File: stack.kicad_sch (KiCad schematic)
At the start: 23 parts, among them U43 74LS193, U46 74LS193, U56 74HCT00, U7 74HCT245

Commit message: changed symbols
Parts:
- U43, U46: symbol 74xx:74LS193 -> 01_my_library:74HCT193
- U7: symbol 74xx:74HC245 -> 01_my_library:74HCT245
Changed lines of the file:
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@@
     )
   )
-  (symbol (lib_id "74xx:74LS193") (at 162.56 104.14 270) (unit 1)
+  (symbol (lib_id "01_my_library:74HCT193") (at 161.29 104.14 270) (unit 1)
     (in_bom yes) (on_board yes) (dnp no) (fields_autoplaced)
     (property "Reference" "U46" (at 180.34 97.2119 90)
@@
       (effects (font (size 1.27 1.27)))
     )
-    (property "Footprint" "" (at 162.56 104.14 0)
-      (effects (font (size 1.27 1.27)) hide)
-    )
-    (property "Datasheet" "http://www.ti.com/lit/ds/symlink/sn74ls193.pdf" (at 162.56 104.14 0)
+    (property "Footprint" "" (at 161.29 104.14 0)
+      (effects (font (size 1.27 1.27)) hide)
+    )
+    (property "Datasheet" "https://www.ti.com/lit/ds/symlink/cd74hct193.pdf?HQS=dis-mous-null-mousermode-dsf-pf-null-wwe&ts=1702791971938&ref_url=https%253A%252F%252Fwww.mouser.be%252F" (at 146.05 104.14 0)
       (effects (font (size 1.27 1.27)) hide)
     )
@@
     )
   )
-  (symbol (lib_id "74xx:74LS193") (at 226.06 104.14 270) (unit 1)
+  (symbol (lib_id "01_my_library:74HCT193") (at 224.79 104.14 270) (unit 1)
     (in_bom yes) (on_board yes) (dnp no) (fields_autoplaced)
     (property "Reference" "U43" (at 243.84 97.2119 90)
@@
       (effects (font (size 1.27 1.27)))
     )
-    (property "Footprint" "" (at 226.06 104.14 0)
-      (effects (font (size 1.27 1.27)) hide)
-    )
-    (property "Datasheet" "http://www.ti.com/lit/ds/symlink/sn74ls193.pdf" (at 226.06 104.14 0)
+    (property "Footprint" "" (at 224.79 104.14 0)
+      (effects (font (size 1.27 1.27)) hide)
+    )
+    (property "Datasheet" "https://www.ti.com/lit/ds/symlink/cd74hct193.pdf?HQS=dis-mous-null-mousermode-dsf-pf-null-wwe&ts=1702791971938&ref_url=https%253A%252F%252Fwww.mouser.be%252F" (at 209.55 104.14 0)
       (effects (font (size 1.27 1.27)) hide)
     )
@@
     )
   )
-  (symbol (lib_id "74xx:74HC245") (at 92.71 104.14 90) (unit 1)
+  (symbol (lib_id "01_my_library:74HCT245") (at 92.71 104.14 90) (unit 1)
     (in_bom yes) (on_board yes) (dnp no)
     (property "Reference" "U7" (at 113.03 97.79 90)
@@
       (effects (font (size 1.27 1.27)) hide)
     )
-    (property "Datasheet" "http://www.ti.com/lit/gpn/sn74HC245" (at 92.71 104.14 0)
-      (effects (font (size 1.27 1.27)) hide)
-    )
+    (property "Datasheet" "https://www.ti.com/lit/ds/symlink/sn74hct245.pdf?ts=1702763405638&ref_url=https%253A%252F%252Fwww.google.com%252F" (at 115.57 104.14 0)
+      (effects (font (size 1.27 1.27)) hide)
+    )

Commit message: some cleanup
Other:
- note added: "I am running out of control signals. I don't see the need to input a stack address, so I am not providing it."
- note removed: "I am running out of control signal. I don't see the need to input a stack address, so I am not providing it."
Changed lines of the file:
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@@
     (stroke (width 0) (type default))
   )
-  (text "I am running out of control signal.\nI don't see the need to input a stack\naddress, so I am not providing it."
+  (text "I am running out of control signals.\nI don't see the need to input a stack\naddress, so I am not providing it."
     (at 245.11 69.85 0)
     (effects (font (size 1.27 1.27)) (justify left bottom))
@@
         )
         (path "/100bb8d1-c3d6-4e1f-87b6-72e4e187243c/77326d47-b417-46cc-a46c-7ab94a8e927d"
-          (reference "#PWR0235") (unit 1)
+          (reference "#PWR0249") (unit 1)
         )
       )
@@
         )
         (path "/100bb8d1-c3d6-4e1f-87b6-72e4e187243c/77326d47-b417-46cc-a46c-7ab94a8e927d"
-          (reference "D118") (unit 1)
+          (reference "D119") (unit 1)
         )
       )
@@
         )
         (path "/100bb8d1-c3d6-4e1f-87b6-72e4e187243c/77326d47-b417-46cc-a46c-7ab94a8e927d"
-          (reference "#PWR0227") (unit 1)
+          (reference "#PWR0241") (unit 1)
         )
       )
@@
         )
         (path "/100bb8d1-c3d6-4e1f-87b6-72e4e187243c/77326d47-b417-46cc-a46c-7ab94a8e927d"
-          (reference "R165") (unit 1)
+          (reference "R166") (unit 1)
         )
       )
@@
         )
         (path "/100bb8d1-c3d6-4e1f-87b6-72e4e187243c/77326d47-b417-46cc-a46c-7ab94a8e927d"
-          (reference "#PWR0234") (unit 1)
+          (reference "#PWR0248") (unit 1)
         )
       )
@@
         )
         (path "/100bb8d1-c3d6-4e1f-87b6-72e4e187243c/77326d47-b417-46cc-a46c-7ab94a8e927d"
-          (reference "R166") (unit 1)
+          (reference "R167") (unit 1)
         )
       )
@@
         )
         (path "/100bb8d1-c3d6-4e1f-87b6-72e4e187243c/77326d47-b417-46cc-a46c-7ab94a8e927d"
-          (reference "R161") (unit 1)
+          (reference "R162") (unit 1)
         )
       )
@@
         )
         (path "/100bb8d1-c3d6-4e1f-87b6-72e4e187243c/77326d47-b417-46cc-a46c-7ab94a8e927d"
-          (reference "#PWR0226") (unit 1)
+          (reference "#PWR0240") (unit 1)
         )
       )
@@
         )
         (path "/100bb8d1-c3d6-4e1f-87b6-72e4e187243c/77326d47-b417-46cc-a46c-7ab94a8e927d"
-          (reference "#PWR0236") (unit 1)
+          (reference "#PWR0250") (unit 1)
         )
       )
@@
         )
         (path "/100bb8d1-c3d6-4e1f-87b6-72e4e187243c/77326d47-b417-46cc-a46c-7ab94a8e927d"
-          (reference "#PWR0228") (unit 1)
+          (reference "#PWR0242") (unit 1)
         )
       )
@@
         )
         (path "/100bb8d1-c3d6-4e1f-87b6-72e4e187243c/77326d47-b417-46cc-a46c-7ab94a8e927d"
-          (reference "D117") (unit 1)
+          (reference "D118") (unit 1)
         )
       )
@@
         )
         (path "/100bb8d1-c3d6-4e1f-87b6-72e4e187243c/77326d47-b417-46cc-a46c-7ab94a8e927d"
-          (reference "#PWR0233") (unit 1)
+          (reference "#PWR0247") (unit 1)
         )
       )
@@
         )
         (path "/100bb8d1-c3d6-4e1f-87b6-72e4e187243c/77326d47-b417-46cc-a46c-7ab94a8e927d"
-          (reference "D116") (unit 1)
+          (reference "D117") (unit 1)
         )
       )
@@
         )
         (path "/100bb8d1-c3d6-4e1f-87b6-72e4e187243c/77326d47-b417-46cc-a46c-7ab94a8e927d"
-          (reference "D119") (unit 1)
+          (reference "D120") (unit 1)
         )
       )
@@
         )
         (path "/100bb8d1-c3d6-4e1f-87b6-72e4e187243c/77326d47-b417-46cc-a46c-7ab94a8e927d"
-          (reference "C64") (unit 1)
+          (reference "C68") (unit 1)
         )
       )
@@
         )
         (path "/100bb8d1-c3d6-4e1f-87b6-72e4e187243c/77326d47-b417-46cc-a46c-7ab94a8e927d"
-          (reference "D115") (unit 1)
+          (reference "D116") (unit 1)
         )
       )
@@
         )
         (path "/100bb8d1-c3d6-4e1f-87b6-72e4e187243c/77326d47-b417-46cc-a46c-7ab94a8e927d"
-          (reference "R164") (unit 1)
+          (reference "R165") (unit 1)
         )
       )
@@
         )
         (path "/100bb8d1-c3d6-4e1f-87b6-72e4e187243c/77326d47-b417-46cc-a46c-7ab94a8e927d"
-          (reference "U58") (unit 1)
+          (reference "U61") (unit 1)
         )
       )
@@
         )
         (path "/100bb8d1-c3d6-4e1f-87b6-72e4e187243c/77326d47-b417-46cc-a46c-7ab94a8e927d"
-          (reference "R162") (unit 1)
+          (reference "R163") (unit 1)
         )
       )
@@
         )
         (path "/100bb8d1-c3d6-4e1f-87b6-72e4e187243c/77326d47-b417-46cc-a46c-7ab94a8e927d"
-          (reference "#PWR0229") (unit 1)
+          (reference "#PWR0243") (unit 1)
         )
       )
@@
         )
         (path "/100bb8d1-c3d6-4e1f-87b6-72e4e187243c/77326d47-b417-46cc-a46c-7ab94a8e927d"
-          (reference "C66") (unit 1)
+          (reference "C70") (unit 1)
         )
       )
@@
         )
         (path "/100bb8d1-c3d6-4e1f-87b6-72e4e187243c/77326d47-b417-46cc-a46c-7ab94a8e927d"
-          (reference "U59") (unit 1)
+          (reference "U62") (unit 1)
         )
       )
@@
         )
         (path "/100bb8d1-c3d6-4e1f-87b6-72e4e187243c/77326d47-b417-46cc-a46c-7ab94a8e927d"
-          (reference "D121") (unit 1)
+          (reference "D122") (unit 1)
         )
       )
@@
         )
         (path "/100bb8d1-c3d6-4e1f-87b6-72e4e187243c/77326d47-b417-46cc-a46c-7ab94a8e927d"
-          (reference "R159") (unit 1)
+          (reference "R160") (unit 1)
         )
       )
@@
         )
         (path "/100bb8d1-c3d6-4e1f-87b6-72e4e187243c/77326d47-b417-46cc-a46c-7ab94a8e927d"
-          (reference "#PWR0237") (unit 1)
+          (reference "#PWR0239") (unit 1)
         )
       )
@@
         )
         (path "/100bb8d1-c3d6-4e1f-87b6-72e4e187243c/77326d47-b417-46cc-a46c-7ab94a8e927d"
-          (reference "#PWR0231") (unit 1)
+          (reference "#PWR0245") (unit 1)
         )
       )
@@
         )
         (path "/100bb8d1-c3d6-4e1f-87b6-72e4e187243c/77326d47-b417-46cc-a46c-7ab94a8e927d"
-          (reference "C65") (unit 1)
+          (reference "C69") (unit 1)
         )
       )
@@
         )
         (path "/100bb8d1-c3d6-4e1f-87b6-72e4e187243c/77326d47-b417-46cc-a46c-7ab94a8e927d"
-          (reference "D120") (unit 1)
+          (reference "D121") (unit 1)
         )
       )
@@
         )
         (path "/100bb8d1-c3d6-4e1f-87b6-72e4e187243c/77326d47-b417-46cc-a46c-7ab94a8e927d"
-          (reference "R160") (unit 1)
+          (reference "R161") (unit 1)
         )
       )
@@
         )
         (path "/100bb8d1-c3d6-4e1f-87b6-72e4e187243c/77326d47-b417-46cc-a46c-7ab94a8e927d"
-          (reference "#PWR0232") (unit 1)
+          (reference "#PWR0246") (unit 1)
         )
       )
@@
         )
         (path "/100bb8d1-c3d6-4e1f-87b6-72e4e187243c/77326d47-b417-46cc-a46c-7ab94a8e927d"
-          (reference "U57") (unit 1)
+          (reference "U60") (unit 1)
         )
       )
@@
         )
         (path "/100bb8d1-c3d6-4e1f-87b6-72e4e187243c/77326d47-b417-46cc-a46c-7ab94a8e927d"
-          (reference "D122") (unit 1)
+          (reference "D123") (unit 1)
         )
       )
@@
         )
         (path "/100bb8d1-c3d6-4e1f-87b6-72e4e187243c/77326d47-b417-46cc-a46c-7ab94a8e927d"
-          (reference "R163") (unit 1)
+          (reference "R164") (unit 1)
         )
       )
@@
         )
         (path "/100bb8d1-c3d6-4e1f-87b6-72e4e187243c/77326d47-b417-46cc-a46c-7ab94a8e927d"
-          (reference "#PWR0230") (unit 1)
-        )
-      )
+          (reference "#PWR0244") (unit 1)
+        )
+      )

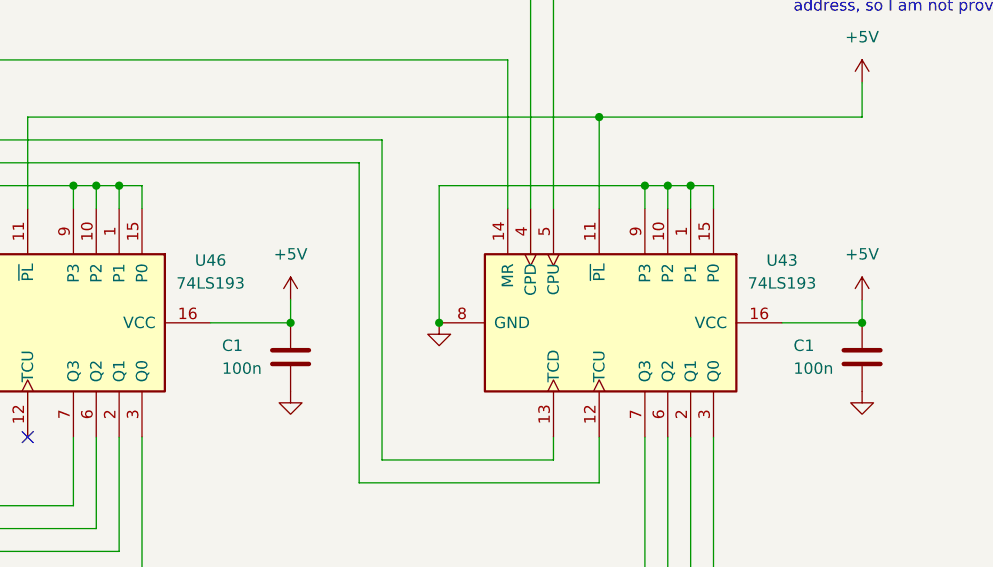
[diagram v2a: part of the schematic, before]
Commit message: add arduino headers for programming
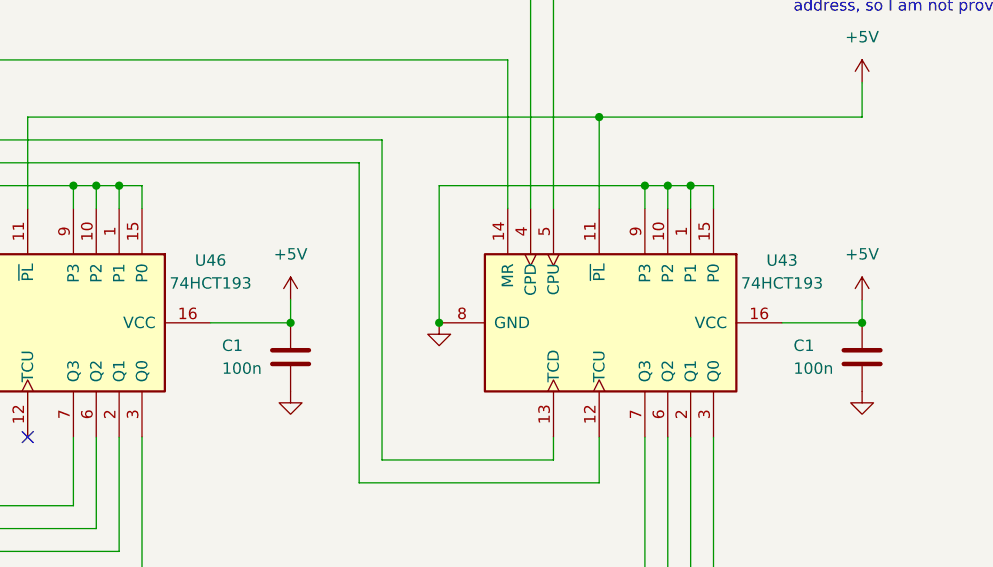
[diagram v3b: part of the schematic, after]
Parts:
- U43, U46: value 74LS193 -> 74HCT193; footprint (none) -> Package_DIP:DIP-16_W7.62mm
- U56: footprint (none) -> Package_DIP:DIP-14_W7.62mm
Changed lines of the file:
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@@
       (effects (font (size 1.27 1.27)))
     )
-    (property "Value" "74LS193" (at 180.34 99.7519 90)
-      (effects (font (size 1.27 1.27)))
-    )
-    (property "Footprint" "" (at 161.29 104.14 0)
+    (property "Value" "74HCT193" (at 180.34 99.7519 90)
+      (effects (font (size 1.27 1.27)))
+    )
+    (property "Footprint" "Package_DIP:DIP-16_W7.62mm" (at 161.29 104.14 0)
       (effects (font (size 1.27 1.27)) hide)
     )
@@
       (effects (font (size 1.27 1.27)))
     )
-    (property "Footprint" "" (at 110.49 25.4 0)
+    (property "Footprint" "Package_DIP:DIP-14_W7.62mm" (at 110.49 25.4 0)
       (effects (font (size 1.27 1.27)) hide)
     )
@@
       (effects (font (size 1.27 1.27)))
     )
-    (property "Footprint" "" (at 110.49 40.64 0)
+    (property "Footprint" "Package_DIP:DIP-14_W7.62mm" (at 110.49 40.64 0)
       (effects (font (size 1.27 1.27)) hide)
     )
@@
       (effects (font (size 1.27 1.27)))
     )
-    (property "Value" "74LS193" (at 243.84 99.7519 90)
-      (effects (font (size 1.27 1.27)))
-    )
-    (property "Footprint" "" (at 224.79 104.14 0)
-      (effects (font (size 1.27 1.27)) hide)
-    )
+    (property "Value" "74HCT193" (at 243.84 99.7519 90)
+      (effects (font (size 1.27 1.27)))
+    )
+    (property "Footprint" "Package_DIP:DIP-16_W7.62mm" (at 224.79 104.14 0)
+      (effects (font (size 1.27 1.27)) hide)
+    )

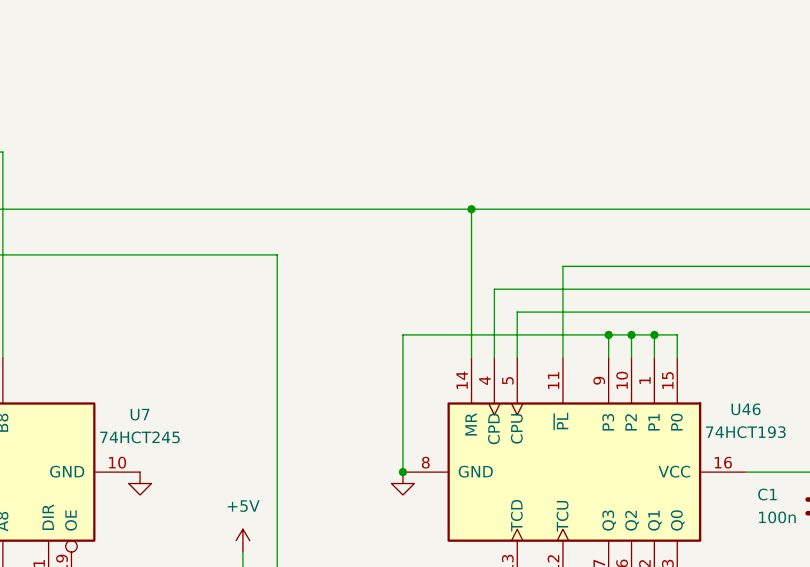
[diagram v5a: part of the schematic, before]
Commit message: fixed push address, push pop tested, fibonacci loops correctly
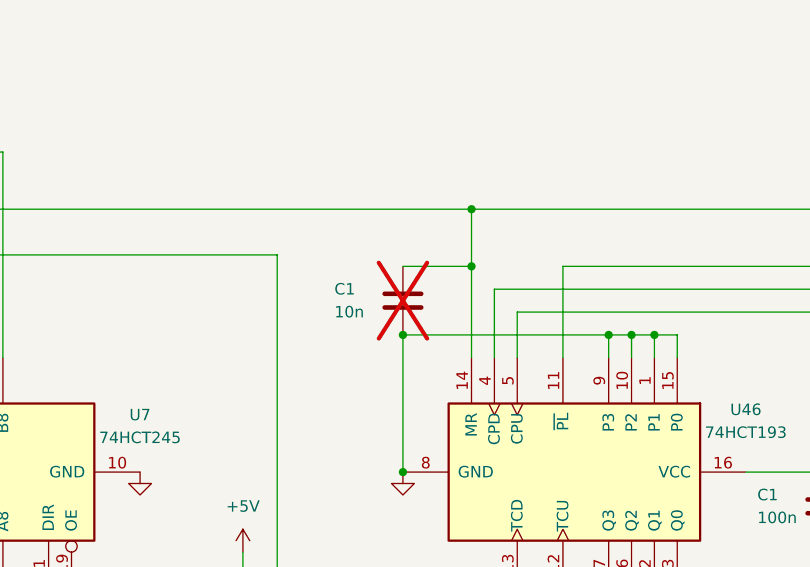
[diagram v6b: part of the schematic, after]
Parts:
- added C1: 10n, 01_my_library:C_Disc_D4.0mm_W2.6mm_P2.50mm, symbol Device:C
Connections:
- net GND: now also C1.2
- net RESET: now also C1.1
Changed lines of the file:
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@@
     (company "TBR Designs")
   )
+  (junction (at 142.24 88.9) (diameter 0) (color 0 0 0 0)
+  )
   (junction (at 167.64 88.9) (diameter 0) (color 0 0 0 0)
   )
@@
   )
   (junction (at 170.18 88.9) (diameter 0) (color 0 0 0 0)
+  )
+  (junction (at 149.86 81.28) (diameter 0) (color 0 0 0 0)
   )
   (junction (at 72.39 104.14) (diameter 0) (color 0 0 0 0)
@@
     (stroke (width 0) (type default) (color 255 0 0 1))
   )
-  (wire (pts (xy 149.86 74.93) (xy 149.86 91.44))
+  (wire (pts (xy 149.86 74.93) (xy 149.86 81.28))
+    (stroke (width 0) (type default) (color 255 0 0 1))
+  )
+  (wire (pts (xy 149.86 81.28) (xy 149.86 91.44))
     (stroke (width 0) (type default) (color 255 0 0 1))
   )
@@
   )
   (wire (pts (xy 154.94 86.36) (xy 154.94 91.44))
+    (stroke (width 0) (type default))
+  )
+  (wire (pts (xy 142.24 81.28) (xy 149.86 81.28))
     (stroke (width 0) (type default))
   )
@@
         )
       )
+    )
+  )
+  (symbol (lib_id "Device:C") (at 142.24 85.09 0) (unit 1)
+    (in_bom yes) (on_board yes) (dnp yes)
+    (property "Reference" "C1" (at 134.62 83.82 0)
+      (effects (font (size 1.27 1.27)) (justify left))
+    )
+    (property "Value" "10n" (at 134.62 86.36 0)
+      (effects (font (size 1.27 1.27)) (justify left))
+    )
+    (property "Footprint" "01_my_library:C_Disc_D4.0mm_W2.6mm_P2.50mm" (at 143.2052 88.9 0)
+      (effects (font (size 1.27 1.27)) hide)
+    )
+    (property "Datasheet" "~" (at 142.24 85.09 0)
+      (effects (font (size 1.27 1.27)) hide)
+    )
+    (pin "2")
+    (pin "1")
+    (instances
+      (project "8-bit-cpu"
+        (path "/100bb8d1-c3d6-4e1f-87b6-72e4e187243c/45eb39c3-c748-461e-8330-08aae1247dee"
+          (reference "C1") (unit 1)
+        )
+        (path "/100bb8d1-c3d6-4e1f-87b6-72e4e187243c/651dfbaf-e340-4976-8216-793c5a5aaa3b"
+          (reference "C13") (unit 1)
+        )
+        (path "/100bb8d1-c3d6-4e1f-87b6-72e4e187243c/3568514a-e420-48fa-9fd5-7a290120765b"
+          (reference "C15") (unit 1)
+        )
+        (path "/100bb8d1-c3d6-4e1f-87b6-72e4e187243c/54bf2e20-7ca1-4029-bb63-3da9aa82cef3"
+          (reference "C63") (unit 1)
+        )
+        (path "/100bb8d1-c3d6-4e1f-87b6-72e4e187243c/77326d47-b417-46cc-a46c-7ab94a8e927d"
+          (reference "C37") (unit 1)
+        )
+      )
